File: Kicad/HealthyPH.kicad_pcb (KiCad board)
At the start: 2 copper layers, 68.6 x 53.4 mm, 62 parts, among them CON1 LB_BarrelJack, P1 CONN_8, P2 WallWartExtension, Q1 TIP122, Q2 TIP122, U1 MCP6241, U2 MCP3901, U3 MC78L05, X1 CRYSTAL

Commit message: layout sent to OshPark
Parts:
- moved TP12 14.9 mm to (202.5, 104.9)
- moved R1 3.62 mm to (188.2, 101.5)
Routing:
- net N-0000026: track 9.15 -> 22.0 mm
- net /Pumps/DownPump: track 28.8 -> 30.2 mm
- net GND: track 5.44 -> 4.83 mm
- net AGND: vias 13 -> 12
- net /Digital Access/~RESET: vias 2 -> 1
- net /Arduino/V+_ARD: vias 4 -> 3
- removed copper zone on B.Cu, net AGND

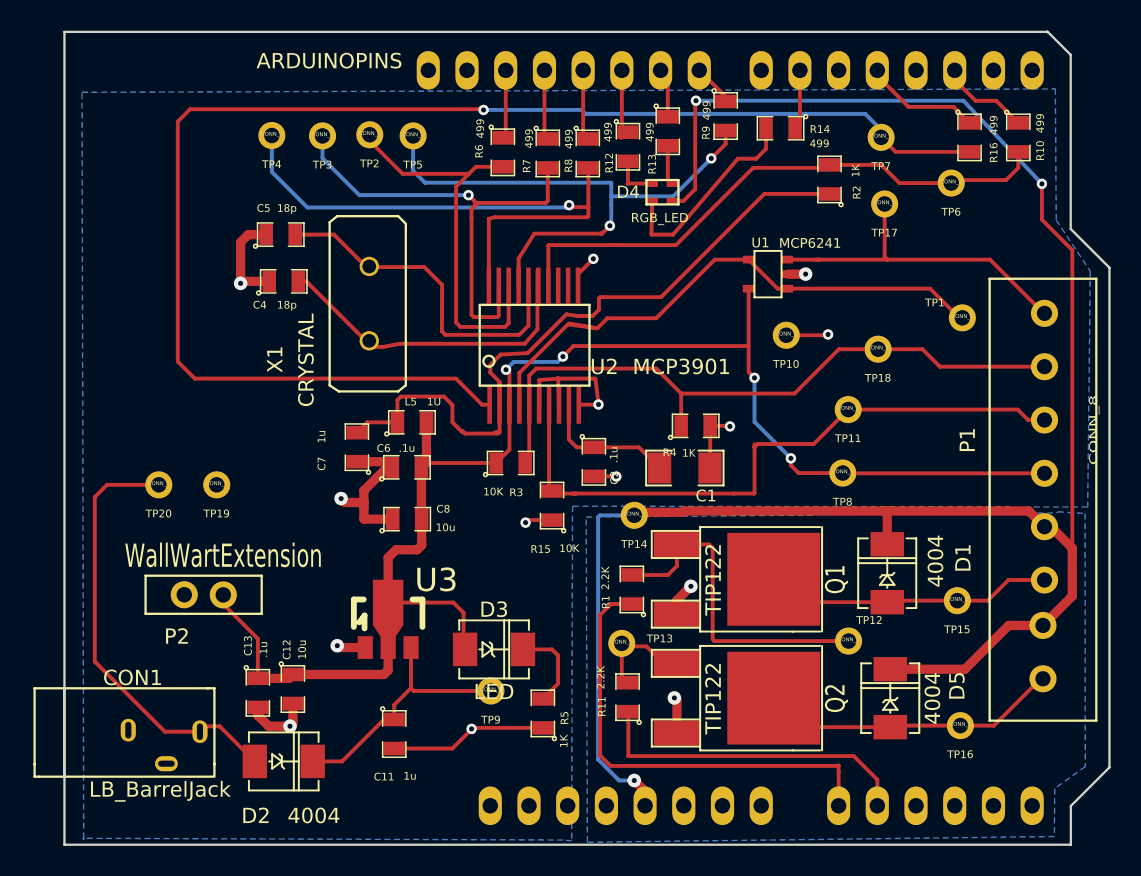
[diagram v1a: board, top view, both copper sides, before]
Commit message: adding diagnostic tests (firmware)
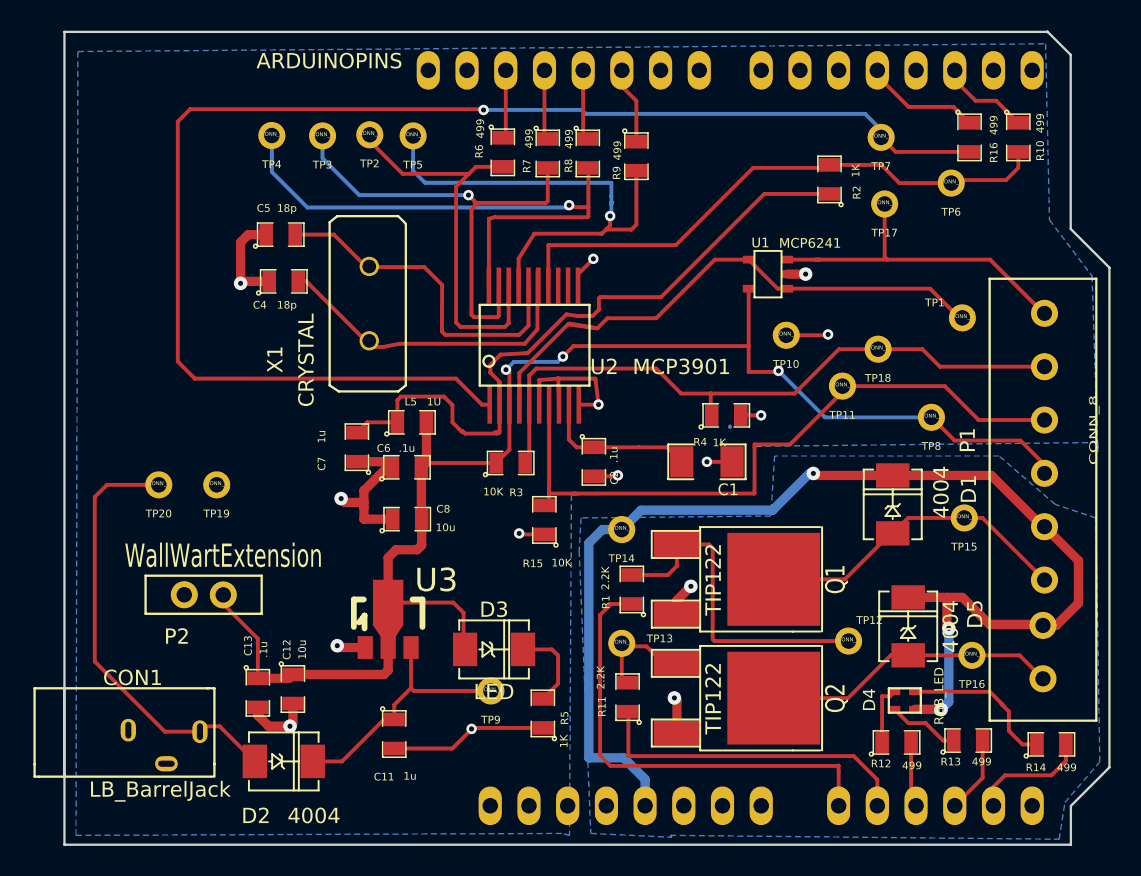
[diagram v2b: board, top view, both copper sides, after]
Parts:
- moved R13 44.6 mm to (210.3, 111.4), turned to 0 degrees
- moved R14 44.2 mm to (215.8, 111.6), turned to 0 degrees
- moved R12 42.9 mm to (205.6, 111.5), turned to 0 degrees
- moved D4 36.9 mm to (205.1, 108.0)
- moved TP8 6.87 mm to (207.9, 90.2)
- moved R9 6.43 mm to (188.5, 73.0)
- moved TP15 5.45 mm to (210.1, 96.8)
- moved D5 4.86 mm to (206.4, 103.9)
- moved TP16 4.67 mm to (210.6, 105.8)
- moved D1 4.53 mm to (205.4, 95.9)
- moved R4 2.12 mm to (194.4, 90.0)
- moved TP11 1.58 mm to (202.1, 88.1)
- moved C1 1.50 mm to (193.2, 93.1)
- moved TP14 1.25 mm to (187.6, 97.5)
- moved R15 1.07 mm to (182.5, 96.9)
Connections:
- ARD1 pad 17: N-0000040 -> (no net)
- ARD1 pad 19: /Arduino/~CS -> (no net)
- ARD1 pad 20: N-0000044 -> (no net)
- ARD1 pad 21: N-0000042 -> /Arduino/~CS
- ARD1 pad 7: (no net) -> N-0000048
- ARD1 pad 8: (no net) -> N-0000045
- ARD1 pad 9: (no net) -> N-0000046
- D4 pad 1: N-0000036 -> N-0000038
- D4 pad 2: N-0000043 -> N-0000037
- D4 pad 3: N-0000045 -> N-0000036
- R12 pad 1: N-0000042 -> N-0000038
- R12 pad 2: N-0000036 -> N-0000048
- R13 pad 1: N-0000044 -> N-0000036
- R13 pad 2: N-0000043 -> N-0000045
- R14 pad 1: N-0000040 -> N-0000037
- R14 pad 2: N-0000045 -> N-0000046
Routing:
- net /Arduino/V+_ARD: track 130.6 -> 81.2 mm
- net N-0000037: track 0.00 -> 10.5 mm
- net N-0000045: track 13.6 -> 5.04 mm
- net N-0000046: track 0.00 -> 7.78 mm
- net N-0000042: track 4.68 -> 0.00 mm
- net N-0000040: track 4.38 -> 0.00 mm
- net N-0000048: track 0.00 -> 4.29 mm
- net /Pumps/SW_DownPump: track 19.0 -> 23.2 mm
- net N-0000038: track 0.00 -> 3.98 mm
- net /Digital Access/~CS_ISO: track 37.3 -> 33.3 mm, vias 2 -> 1
- net N-0000044: track 3.24 -> 0.00 mm
- net N-0000043: track 2.60 -> 0.00 mm
- net /Temperature/10K Therm: track 42.9 -> 45.5 mm
- net /Pumps/SW_UpPump: track 20.7 -> 23.3 mm
- net /Arduino/~CS: track 2.77 -> 5.08 mm
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- added copper zone on B.Cu, net AGND

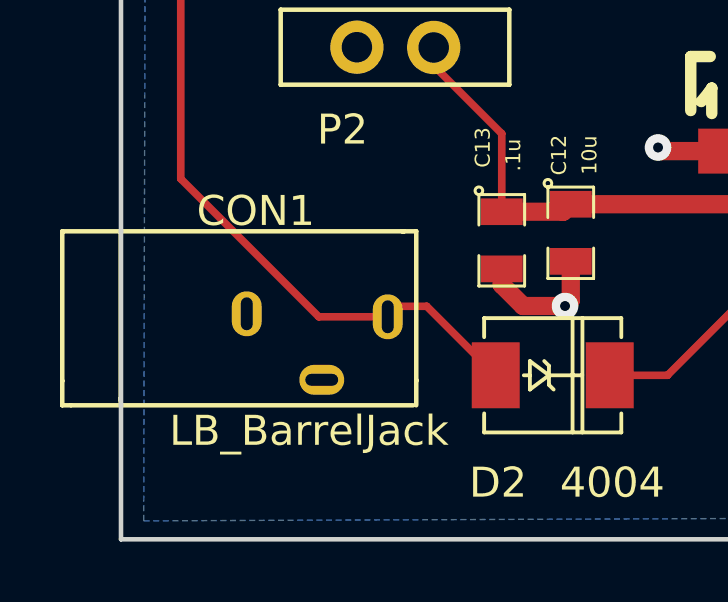
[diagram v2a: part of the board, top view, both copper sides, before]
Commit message: updated to include SPI tests
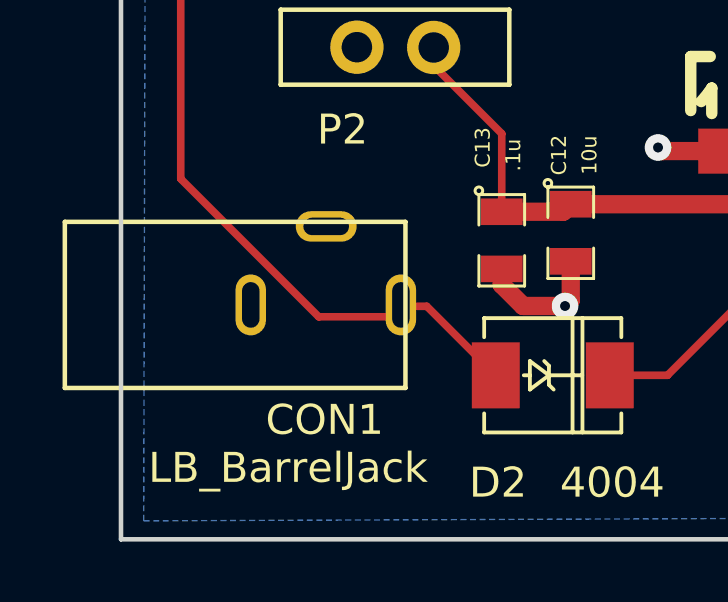
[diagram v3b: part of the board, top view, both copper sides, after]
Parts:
- CON1: footprint LB_BarrelJack -> LB_BarrelJack_Correct
- moved CON1 0.39 mm to (149.1, 107.6)
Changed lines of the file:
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@@
   (general
     (links 109)
-    (no_connects 0)
-    (area 144.330999 64.530999 219.919001 118.704)
+    (no_connects 18)
+    (area 144.330999 64.530999 234.650083 127.331081)
     (thickness 1.6)
     (drawings 10)
@@
     (mod_text_size 1 1)
     (mod_text_width 0.15)
-    (pad_size 1.778 1.778)
-    (pad_drill 1.016)
+    (pad_size 2.032 1.016)
+    (pad_drill 1.524)
     (pad_to_mask_clearance 0)
     (aux_axis_origin 0 0)
@@
     )
   )
-  (module LB_BarrelJack (layer F.Cu)
-    (at 149 108)
-    (fp_text reference CON1 (at 6.5 -0.725) (layer F.SilkS)
-      (effects (font (size 1 1) (thickness 0.15)))
-    )
-    (fp_text value LB_BarrelJack (at 8.276 6.604) (layer F.SilkS)
-      (effects (font (size 1 1) (thickness 0.15)))
-    )
-    (fp_line (start 2 5.5) (end 2 5.7) (layer F.SilkS) (width 0.15))
-    (fp_line (start 2 0) (end 2 5.6) (layer F.SilkS) (width 0.15))
-    (fp_line (start 0.05 4.925) (end 0.05 5.75) (layer F.SilkS) (width 0.15))
-    (fp_line (start 0.05 5.75) (end 0.325 5.75) (layer F.SilkS) (width 0.15))
-    (fp_line (start 11.375 -0.05) (end 11.85 -0.05) (layer F.SilkS) (width 0.15))
-    (fp_line (start 11.85 4.9) (end 11.85 5.75) (layer F.SilkS) (width 0.15))
-    (fp_line (start 0.35 5.75) (end 11.75 5.75) (layer F.SilkS) (width 0.15))
-    (fp_line (start 11.85 4.95) (end 11.85 -0.05) (layer F.SilkS) (width 0.15))
-    (fp_line (start 11.45 -0.05) (end 0.05 -0.05) (layer F.SilkS) (width 0.15))
-    (fp_line (start 0.05 -0.05) (end 0.05 4.95) (layer F.SilkS) (width 0.15))
-    (pad 2 thru_hole oval (at 6.2 2.7 180) (size 1 1.5) (drill oval 0.4 1.1)
-      (layers *.Cu *.Mask F.SilkS)
-      (net 23 AGND)
-    )
-    (pad 3 thru_hole oval (at 8.7 4.9 180) (size 1.5 1) (drill oval 1.1 0.4)
-      (layers *.Cu *.Mask F.SilkS)
-      (net 23 AGND)
-    )
-    (pad 1 thru_hole oval (at 10.9 2.8 180) (size 1 1.5) (drill oval 0.4 1.1)
-      (layers *.Cu *.Mask F.SilkS)
-      (net 33 N-0000035)
-    )
-  )
   (module SM0805 (layer F.Cu)
     (at 215.773 111.633)
@@
     )
   )
+  (module LB_BarrelJack_Correct (layer F.Cu)
+    (at 149.1361 107.63504)
+    (fp_text reference CON1 (at 8.6614 6.604) (layer F.SilkS)
+      (effects (font (size 1 1) (thickness 0.15)))
+    )
+    (fp_text value LB_BarrelJack (at 7.4422 8.2042) (layer F.SilkS)
+      (effects (font (size 1 1) (thickness 0.15)))
+    )
+    (fp_line (start 0 0) (end 11.3538 0) (layer F.SilkS) (width 0.15))
+    (fp_line (start 11.3538 0) (end 11.3538 5.5372) (layer F.SilkS) (width 0.15))
+    (fp_line (start 11.3538 5.5372) (end 0 5.5372) (layer F.SilkS) (width 0.15))
+    (fp_line (start 0 5.5372) (end 0 0) (layer F.SilkS) (width 0.15))
+    (pad 1 thru_hole oval (at 11.2014 2.7686) (size 1.016 2.032) (drill oval 0.5842 1.524)
+      (layers *.Cu *.Mask F.SilkS)
+      (net 33 N-0000035)
+    )
+    (pad 2 thru_hole oval (at 6.1976 2.7686) (size 1.016 2.032) (drill oval 0.5842 1.524)
+      (layers *.Cu *.Mask F.SilkS)
+      (net 23 AGND)
+    )
+    (pad 3 thru_hole oval (at 8.7122 0.1524) (size 2.032 1.016) (drill oval 1.524 0.5842)
+      (layers *.Cu *.Mask F.SilkS)
+      (net 23 AGND)
+    )
+  )

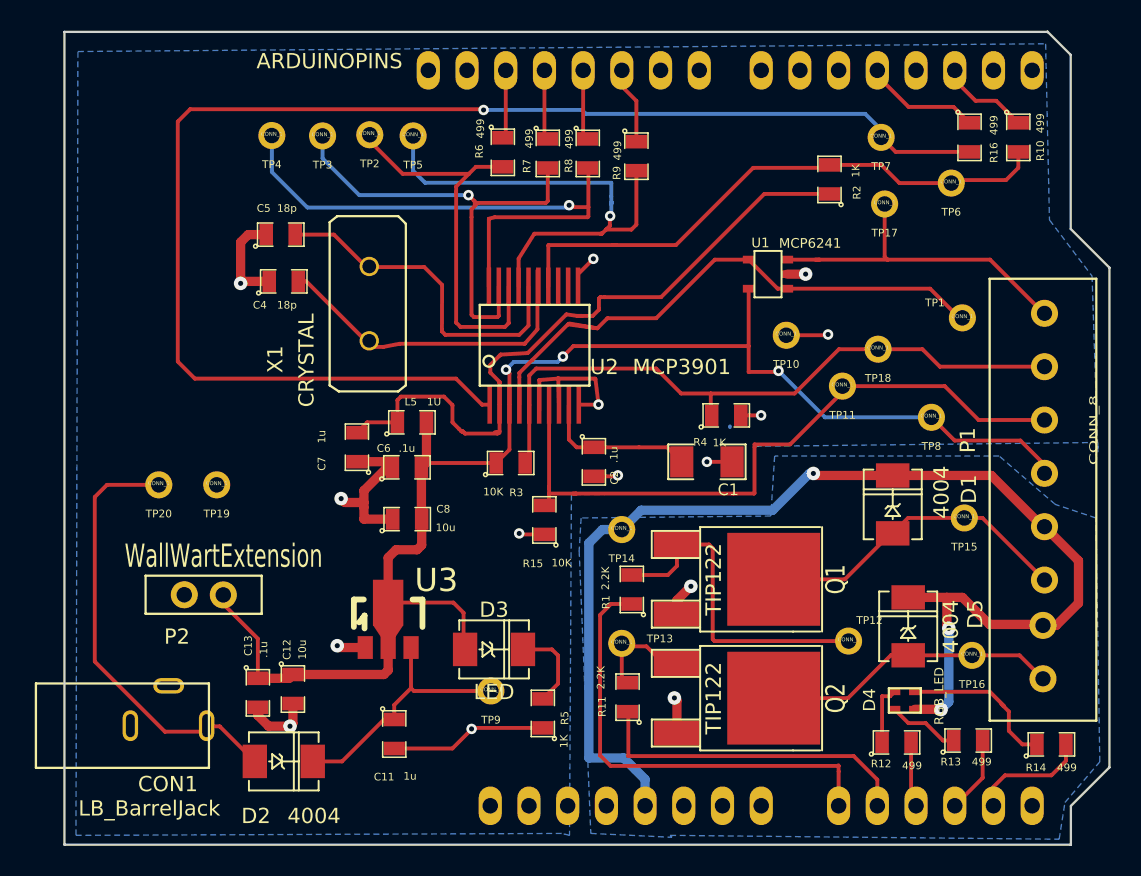
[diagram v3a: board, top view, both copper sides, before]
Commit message: updated with changes for pH volt testing in mcp3901
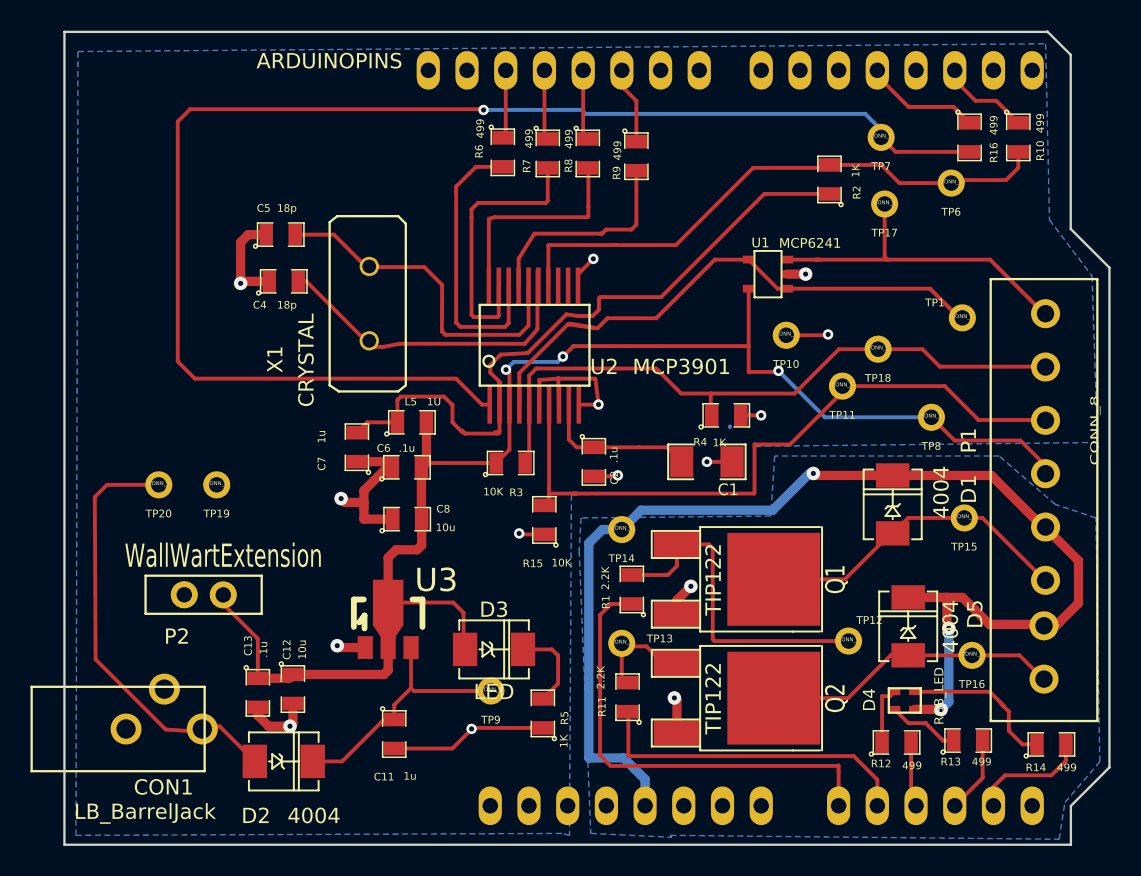
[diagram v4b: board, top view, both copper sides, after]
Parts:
- removed TP2, TP3, TP4, TP5: CONN_1, LB_TestPoint
- moved CON1 0.36 mm to (148.9, 107.9)
- moved P1 0.07 mm to (218.8, 81.1)
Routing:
- net /Digital Access/MOSI_ISO: track 38.5 -> 14.2 mm, vias 1 -> 0
- net /Digital Access/~CS_ISO: track 33.3 -> 14.3 mm, vias 1 -> 0
- net /Digital Access/MISO_ISO: track 31.1 -> 18.1 mm, vias 1 -> 0
- net /Digital Access/SCLK_ISO: track 26.3 -> 18.6 mm

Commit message: Ready for Rev3 First layout review
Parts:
- removed ARD1: ARDUINOPINS, ArduinoLettuceBuddy
- removed TP10, TP11, TP12, TP13, TP14, TP15, TP16, TP17, TP18, TP19, TP6, TP7, TP8, TP9: CONN_1, LB_TestPoint
- added ?: , ArduinoLettuceBuddy, F.Cu at (150.9, 118.1)
- added ?: , Ladybug_small, F.Cu at (155.6, 69.9)
- added C3: .1, SM0805, F.Cu at (206.1, 86.9)
- D4: value RGB_LED -> LB_RGBLED
- R15: value 10K -> 1K
- moved R3 28.9 mm to (207.7, 84.0), turned to 90 degrees
- moved R5 25.2 mm to (162.9, 93.6), turned to 270 degrees
- moved R15 24.7 mm to (206.0, 89.4), turned to 0 degrees
- moved D3 24.5 mm to (157.4, 94.1)
- moved TP20 21.2 mm to (169.8, 111.6)
- moved R16 17.8 mm to (192.6, 71.8)
- moved R10 16.9 mm to (196.7, 71.9)
- moved U2 16.5 mm to (193.9, 77.6)
- moved C2 15.4 mm to (200.4, 88.5)
- moved R2 14.7 mm to (190.1, 84.2)
- moved C6 13.3 mm to (184.9, 86.7)
- moved L5 13.3 mm to (185.2, 83.7), turned to 270 degrees
- moved C7 13.3 mm to (181.6, 85.4)
- moved C8 13.3 mm to (184.9, 90.1)
- moved R4 11.3 mm to (204.0, 83.9), turned to 270 degrees
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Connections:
- C12 pad 1: /Digital Access/V+_WallWart -> V+_Clean
- C13 pad 1: /Digital Access/V+_WallWart -> V+_Clean
- C6 pad 2: /Digital Access/V+_WallWart -> V+_Clean
- C8 pad 2: /Digital Access/V+_WallWart -> V+_Clean
- D3 pad 1: /Digital Access/V+_WallWart -> V+_Clean
- L5 pad 2: /Digital Access/V+_WallWart -> V+_Clean
- P1 pad 3: /Temperature/10K Therm -> V+_Clean
- P1 pad 4: /Digital Access/V+_WallWart -> /Temperature/10K Therm
- P2 pad 2: /Digital Access/V+_WallWart -> V+_Clean
- R3 pad 1: /Digital Access/V+_WallWart -> V+_Clean
- U1 pad 5: /Digital Access/V+_WallWart -> V+_Clean
- U2 pad 3: /Digital Access/V+_WallWart -> V+_Clean
- U3 pad 1: AGND -> V+_Clean
- U3 pad 2: /Digital Access/V+_WallWart -> AGND
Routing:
- net V+_Clean: track 0.00 -> 163.3 mm
- net /Digital Access/V+_WallWart: track 99.2 -> 0.00 mm, vias 3 -> 0
- net /Digital Access/~RESET: track 91.1 -> 13.2 mm, vias 1 -> 2
- net N-0000031: track 46.0 -> 18.6 mm
- net /Digital Access/pH_ADC-: track 44.6 -> 21.7 mm
- net /Digital Access/pH_ADC+: track 37.8 -> 16.5 mm
- net /Digital Access/~DR: track 38.3 -> 18.2 mm
- net N-0000028: track 21.8 -> 40.8 mm
- net N-0000026: track 22.0 -> 7.06 mm
- net N-0000035: track 28.2 -> 14.5 mm
- net N-0000027: track 22.6 -> 36.1 mm
- net /pH/pH_Probe_V: track 22.4 -> 11.9 mm
- net N-0000040: track 10.5 -> 3.39 mm
- net /Arduino/V+_ARD: track 81.2 -> 87.3 mm, vias 3 -> 1
- net /Temperature/10K Therm: track 45.5 -> 40.0 mm
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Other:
- board text added: "Healthy pH Dev-rev3"

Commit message: updated based on feedback. Ready for second review
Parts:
- removed the ? at (150.9, 118.1)
- added ARD1: ARDUINOPINS, ArduinoLettuceBuddy, F.Cu at (151.1, 118.2)
- added C10: .1, SM0805, F.Cu at (208.7, 81.3)
- added C9: .1, SM0805, F.Cu at (194.5, 79.4)
- moved C4 26.5 mm to (188.5, 77.0), turned to 180 degrees
- moved C5 18.7 mm to (181.8, 77.2)
- moved R8 17.3 mm to (168.6, 77.4)
- moved C8 14.2 mm to (170.9, 91.8), turned to 270 degrees
- moved U2 13.9 mm to (181.3, 83.5)
- moved U1 12.2 mm to (198.6, 86.2)
- moved C6 12.0 mm to (174.0, 91.8), turned to 270 degrees
- moved R9 11.7 mm to (177.7, 77.3)
- moved R7 11.5 mm to (172.1, 77.3)
- moved X1 11.5 mm to (179.3, 75.5), turned to 0 degrees
- moved R2 10.8 mm to (179.4, 85.2)
- moved L5 10.4 mm to (178.2, 91.4), turned to 180 degrees
- moved C2 10.0 mm to (190.8, 91.3), turned to 0 degrees
- moved R3 7.32 mm to (200.8, 81.5), turned to 270 degrees
- moved R6 6.63 mm to (174.9, 77.2)
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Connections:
- C12 pad 1: V+_Clean -> /Digital Access/V+_WallWart
- C13 pad 1: V+_Clean -> /Digital Access/V+_WallWart
- C3 pad 1: V+_Clean -> /Digital Access/V+_WallWart
- C6 pad 2: V+_Clean -> /Digital Access/V+_WallWart
- C8 pad 2: V+_Clean -> /Digital Access/V+_WallWart
- D3 pad 1: V+_Clean -> /Digital Access/V+_WallWart
- L5 pad 2: V+_Clean -> /Digital Access/V+_WallWart
- P1 pad 1: /pH/pH_Probe_V -> /Digital Access/pH_ADC-
- P1 pad 2: /Digital Access/pH_ADC- -> /pH/pH_Probe_V
- P1 pad 3: V+_Clean -> /Temperature/10K Therm
- P1 pad 4: /Temperature/10K Therm -> /Digital Access/V+_WallWart
- P2 pad 2: V+_Clean -> /Digital Access/V+_WallWart
- R3 pad 1: V+_Clean -> /Digital Access/V+_WallWart
- U1 pad 5: V+_Clean -> /Digital Access/V+_WallWart
- U2 pad 3: V+_Clean -> /Digital Access/V+_WallWart
- U2 pad 4: /Digital Access/pH_ADC+ -> /Digital Access/pH_ADC-
- U2 pad 5: /Digital Access/pH_ADC- -> /Digital Access/pH_ADC+
- U3 pad 1: V+_Clean -> /Digital Access/V+_WallWart
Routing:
- net V+_Clean: track 163.3 -> 0.00 mm
- net /Digital Access/V+_WallWart: track 0.00 -> 145.6 mm
- net N-0000028: track 40.8 -> 10.0 mm
- net N-0000027: track 36.1 -> 10.4 mm
- net /Arduino/MOSI: track 4.82 -> 22.2 mm, vias 0 -> 1
- net /Digital Access/pH_ADC-: track 21.7 -> 38.5 mm
- net /Digital Access/~RESET: track 13.2 -> 26.3 mm, vias 2 -> 0
- net /Arduino/~CS: track 5.08 -> 16.5 mm
- net /Arduino/MISO: track 4.91 -> 15.3 mm, vias 0 -> 1
- net /Digital Access/SCLK_ISO: track 21.7 -> 11.9 mm
- net /Digital Access/pH_ADC+: track 16.5 -> 24.9 mm
- net /Arduino/SCLK: track 4.51 -> 11.1 mm
- net N-0000029: track 18.6 -> 13.1 mm
- net /Digital Access/MOSI_ISO: track 11.5 -> 16.5 mm, vias 2 -> 0
- net /pH/pH_Probe_V: track 11.9 -> 16.1 mm
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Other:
- net class Normal added: clearance 0.254, trace_width 0.254, via_dia 0.6858, via_drill 0.3302

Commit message: Layout sent to OshPark
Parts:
- ~: renamed from ARD1; value ARDUINOPINS -> ~
- moved C10 10.9 mm to (197.9, 79.5), turned to 90 degrees
- moved C9 4.29 mm to (194.8, 83.7)
- moved D1 2.86 mm to (205.2, 98.7)
- moved TP1 1.70 mm to (202.5, 84.9)
- moved D5 0.58 mm to (206.9, 104.0), turned to 0 degrees
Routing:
- net /Digital Access/V+_WallWart: track 145.6 -> 152.0 mm
- net /Arduino/V+_ARD: track 87.5 -> 93.6 mm, vias 1 -> 0
- net /Pumps/SW_DownPump: track 23.2 -> 20.1 mm
- net AGND: track 59.2 -> 61.4 mm
- net /Pumps/SW_UpPump: track 23.3 -> 25.1 mm
- net /Digital Access/pH_ADC+: track 24.9 -> 23.1 mm
